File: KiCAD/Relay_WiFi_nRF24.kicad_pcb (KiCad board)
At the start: 2 copper layers, 50.8 x 50.8 mm, 15 parts, among them IC1 MOC3061M, P1 CONN_4, P2 CONN_4, P3 CONN_01X04, U1 ESP8266-ESP-03, U2 NCP1117ST33T3G, U3 NRF24L01P_SMD, U4 TRIAC

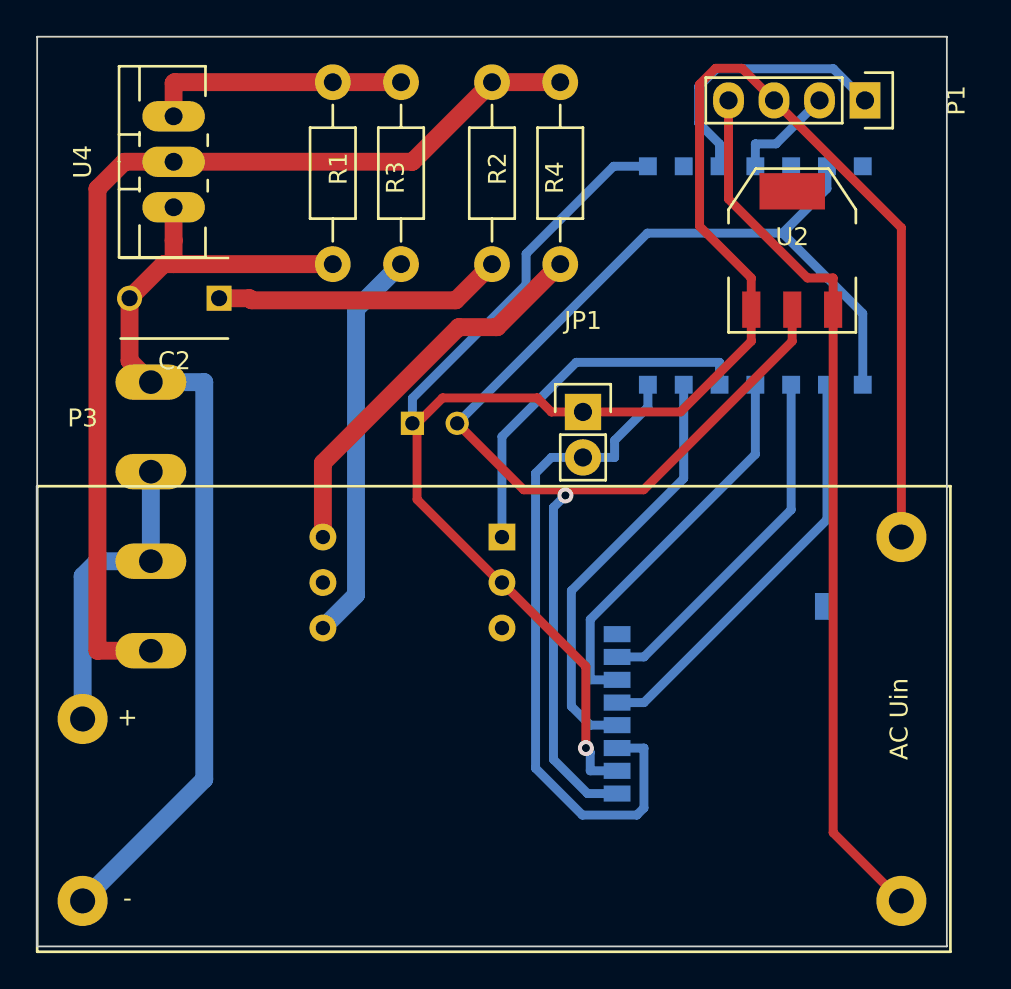
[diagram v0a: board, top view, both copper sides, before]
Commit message: Замена посадочного места блока питания 5V
Изменил посадочное место блока питания под размеры китайского БП с
Ebay.com AC/DC-5V-700A
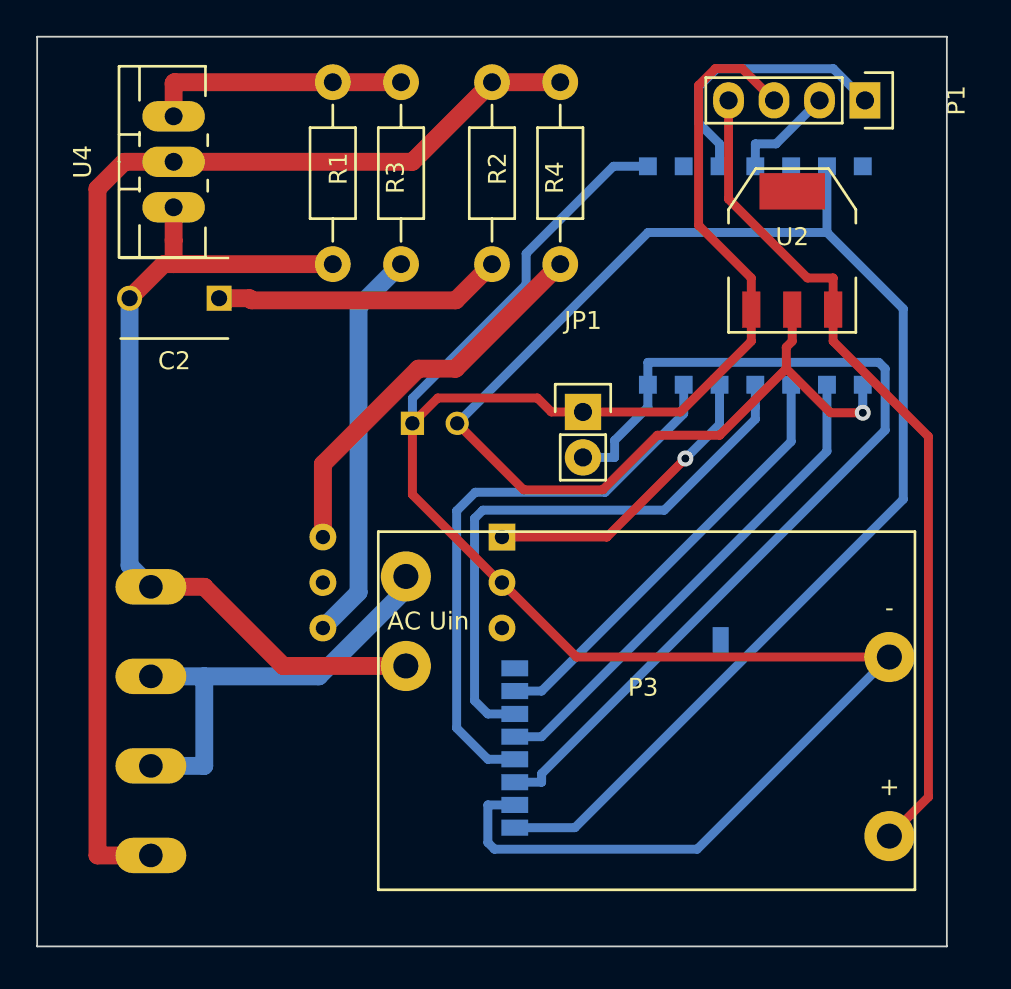
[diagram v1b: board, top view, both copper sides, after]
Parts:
- P3: footprint Converters_DCDC_ACDC:ACDC-Converter_TRACO-TMLM-05 -> Relay_WiFi_nRF24_Libs:ACDC-FromEbay-5V-700A
- moved P3 19.2 mm to (185.4, 158.8)
- moved P2 11.4 mm to (170.2, 163.8)
- moved U3 6.02 mm to (190.5, 163.8)
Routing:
- net Net-(C1-Pad2): track 82.8 -> 107.7 mm
- net Net-(JP1-Pad2): track 38.2 -> 53.8 mm
- net GND: track 115.5 -> 128.2 mm, vias 1 -> 0
- net Net-(P2-Pad1): track 57.1 -> 68.5 mm
- net Net-(U1-Pad11): track 21.8 -> 32.6 mm
- net Net-(U1-Pad13): track 23.5 -> 32.6 mm
- net Net-(P2-Pad2): track 17.1 -> 25.0 mm
- net Net-(C2-Pad2): track 55.3 -> 48.0 mm
- net Net-(U1-Pad10): track 20.1 -> 24.4 mm
- net Net-(U1-Pad9): track 23.5 -> 27.8 mm
- net Net-(IC1-Pad1): track 20.7 -> 17.0 mm, vias 0 -> 1
- net VCC: track 49.5 -> 47.5 mm

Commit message: Правка схемы
Добавлены недостающие подтягивающие резисторы.
Исправлена библиотека посадочного места коннектора для подключения сети
и нагрузки.
Исправлена толщина дорожек.
Уменьшен размер платы.
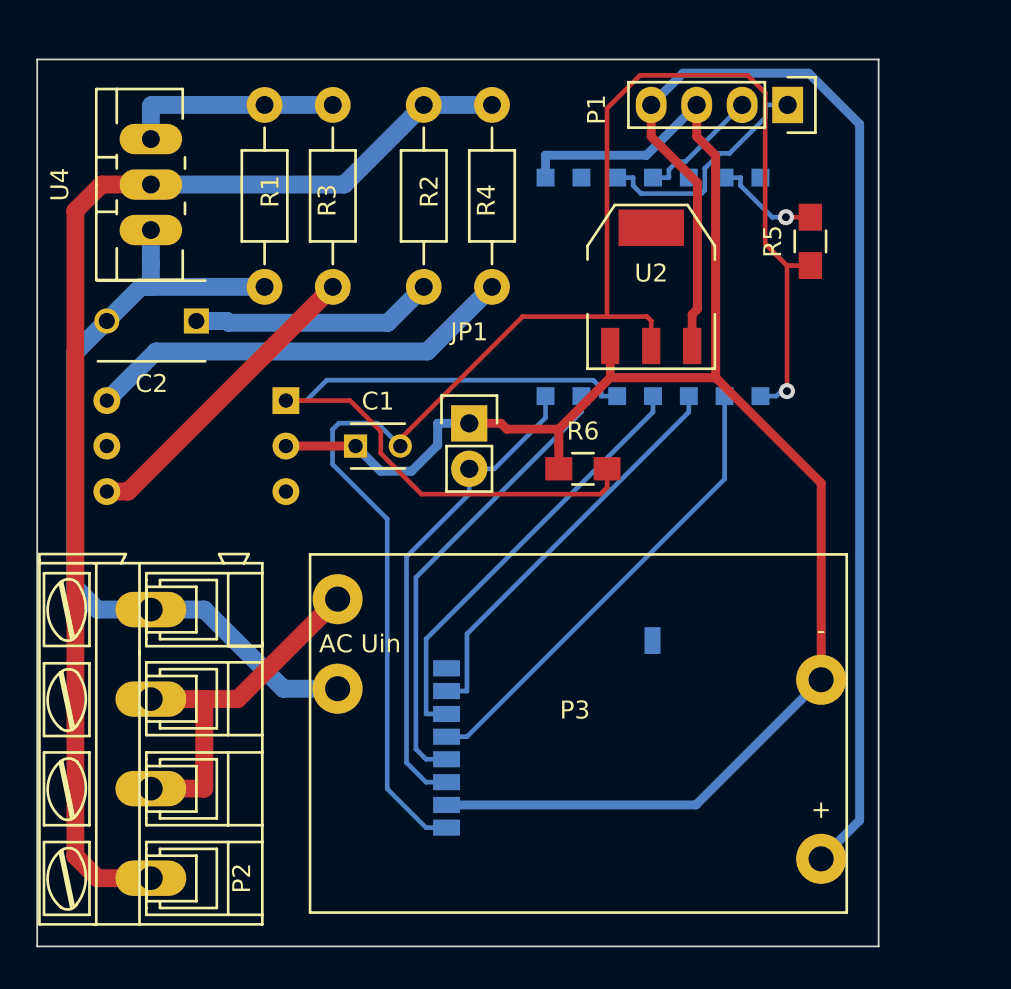
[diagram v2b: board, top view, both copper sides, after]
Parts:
- added R5: 10k, Resistors_SMD:R_0805_HandSoldering, F.Cu at (207.0, 129.5)
- added R6: 10k, Resistors_SMD:R_0805_HandSoldering, F.Cu at (194.3, 142.2)
- C1: moved to F.Cu
- P2: footprint Connect:AK300-4 -> Relay_WiFi_nRF24_Libs:Connector-4; moved to F.Cu
- moved IC1 14.3 mm to (172.7, 141.0)
- moved U2 8.13 mm to (198.1, 132.1)
- moved JP1 6.38 mm to (188.0, 139.7)
- moved U1 5.75 mm to (198.1, 132.1)
- moved P1 4.33 mm to (205.7, 121.9)
- moved R1 4.02 mm to (180.3, 127.0)
- moved R2 4.02 mm to (189.2, 127.0)
- moved R3 4.02 mm to (176.5, 127.0)
- moved R4 4.02 mm to (185.4, 127.0)
- moved P3 4.02 mm to (181.6, 160.0)
- moved U3 3.81 mm to (186.7, 163.8)
- moved C1 3.42 mm to (181.6, 141.0)
- moved C2 1.80 mm to (172.7, 134.0)
- moved U4 1.80 mm to (170.2, 126.4)
- moved P2 1.27 mm to (170.2, 165.1)
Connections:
- U1 pad 6: Net-(C1-Pad2) -> Net-(R5-Pad2)
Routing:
- net GND: track 128.2 -> 101.4 mm
- net Net-(JP1-Pad2): track 53.8 -> 27.2 mm
- net Net-(IC1-Pad1): track 17.0 -> 41.6 mm, vias 1 -> 0
- net VCC: track 47.5 -> 70.1 mm
- net Net-(C1-Pad2): track 107.7 -> 90.4 mm
- net Net-(U1-Pad11): track 32.6 -> 24.1 mm
- net Net-(U1-Pad13): track 32.6 -> 25.5 mm
- net Net-(R5-Pad2): track 0.00 -> 5.97 mm, vias 0 -> 1
- net Net-(IC1-Pad4): track 22.1 -> 17.4 mm
- net Net-(P2-Pad2): track 25.0 -> 20.7 mm
- net Net-(C2-Pad2): track 48.0 -> 45.4 mm
- net Net-(C2-Pad1): track 16.1 -> 13.6 mm
- net Net-(R1-Pad2): track 14.6 -> 12.0 mm
- net Net-(IC1-Pad6): track 22.0 -> 24.1 mm
- net Net-(P2-Pad1): track 68.5 -> 66.5 mm
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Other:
- board size 50.8 x 50.8 mm -> 47 x 49.5 mm

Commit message: Изменения в схеме
Добавлен токоограничивающий резистр.
Мелкие правки печатной платы.
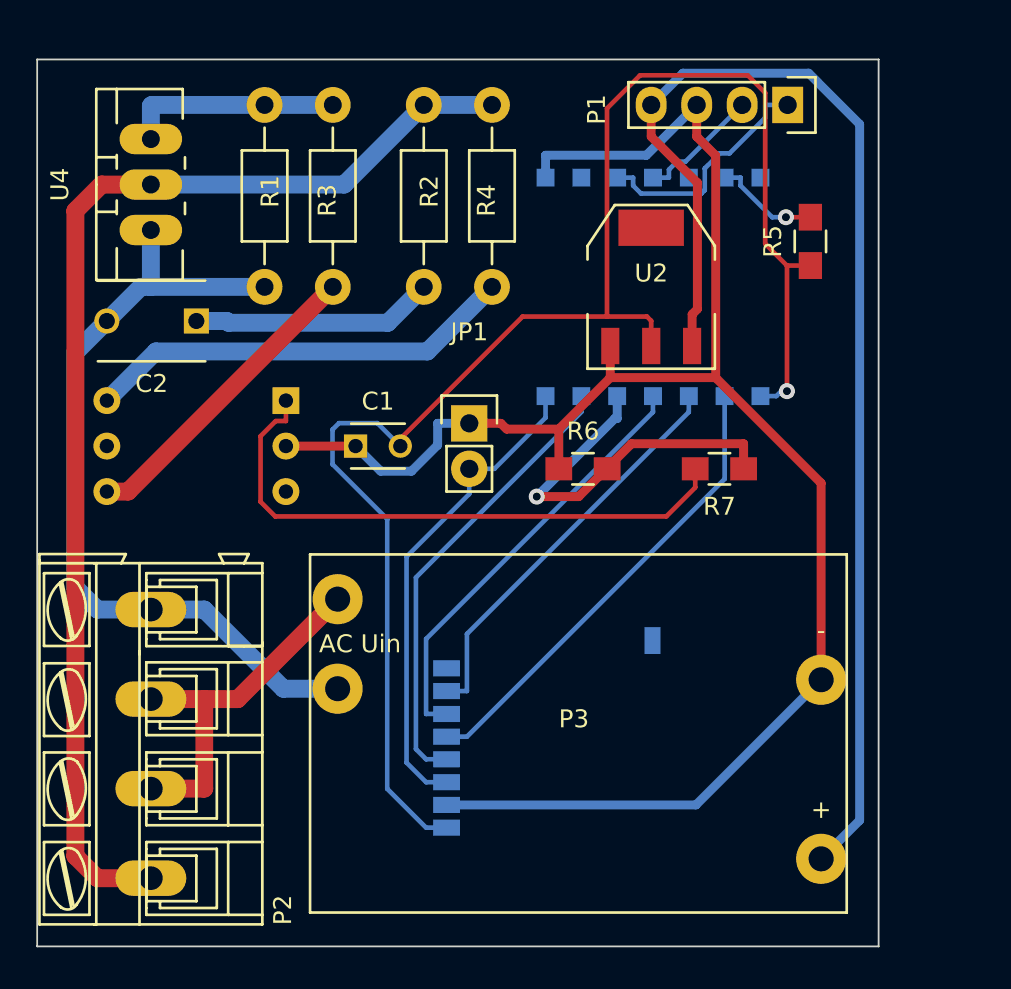
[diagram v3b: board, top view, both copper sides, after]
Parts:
- added R7: 220, Resistors_SMD:R_0805_HandSoldering, F.Cu at (201.9, 142.2)
- P2: footprint Relay_WiFi_nRF24_Libs:Connector-4 -> Connect:AK300-4
- R1: value 360 -> 10k
- R4: value 360 -> 39
- U4: value TRIAC -> BTA16
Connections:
- R6 pad 2: Net-(IC1-Pad1) -> Net-(R6-Pad2)
- U1 pad 12: Net-(IC1-Pad1) -> Net-(R6-Pad2)
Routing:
- net Net-(R6-Pad2): track 0.00 -> 21.8 mm, vias 0 -> 1
- net Net-(IC1-Pad1): track 41.6 -> 32.9 mm

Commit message: [Схема] Надпись на печатной плате
Просто добавил надпись
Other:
- board text added: "Relay board V0.1"
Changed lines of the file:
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@@
     (area 163.779999 119.329999 210.870001 168.960001)
     (thickness 1.6)
-    (drawings 4)
+    (drawings 5)
     (tracks 164)
     (zones 0)
@@
     )
   )
+  (gr_text "Relay board V0.1" (at 195.326 147.828) (layer B.SilkS)
+    (effects (font (size 1.5 1.5) (thickness 0.3)) (justify mirror))
+  )
   (gr_line (start 163.83 168.91) (end 163.83 119.38) (angle 90) (layer Edge.Cuts) (width 0.1))
